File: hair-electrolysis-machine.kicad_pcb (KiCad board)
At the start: 2 copper layers, 53 x 53 mm, 98 parts, among them J1 USB_C_Receptacle_USB2.0_16P, J3 AudioJack2_Ground_Switch, J4 Conn_01x03_Pin, J5 Conn_01x03_Pin, J6 Conn_02x04_Odd_Even, J7 AudioJack2_Ground_Switch, Q1 BSS138, SW3 SW_SPDT, SW4 RotaryEncoder_Switch, SW5 RESET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

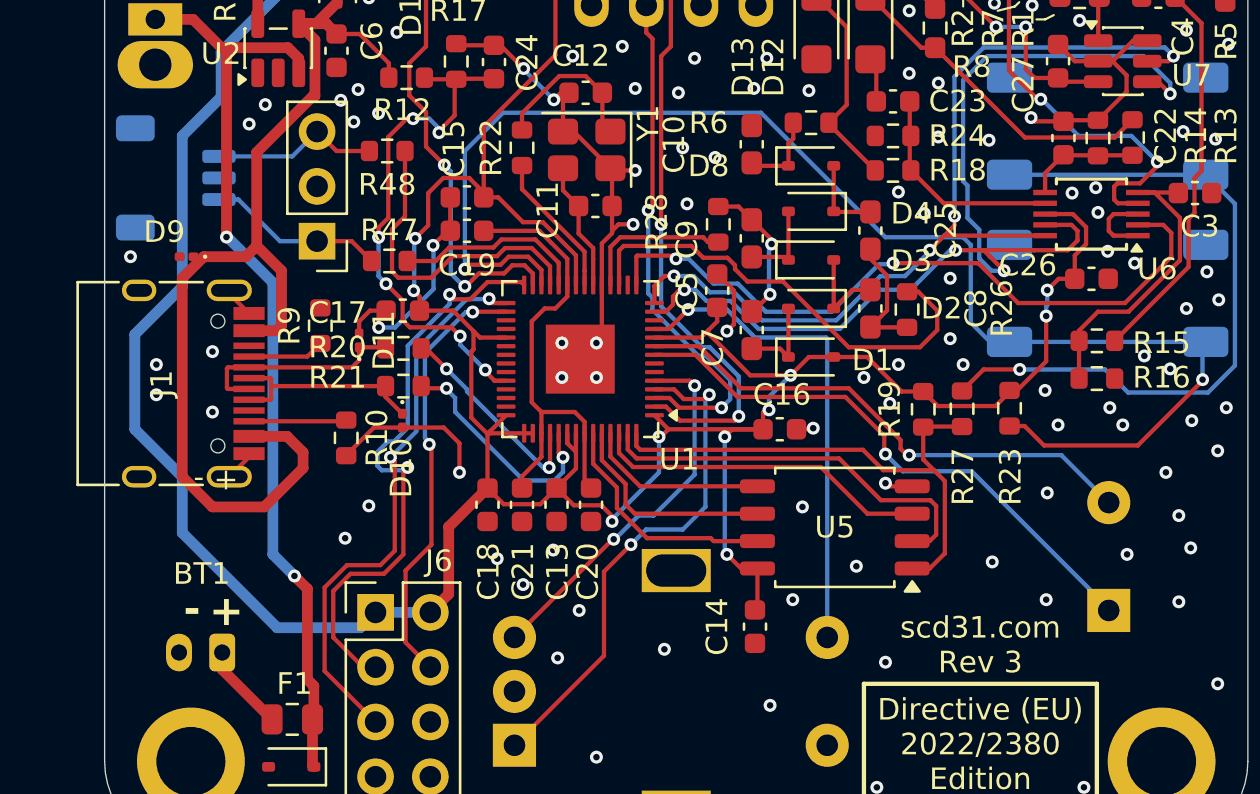
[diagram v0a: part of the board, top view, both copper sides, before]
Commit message: Minor changes
Moved 5v line out from under USB-C connector and changed buzzer pads so more common buzzers can more easily be used
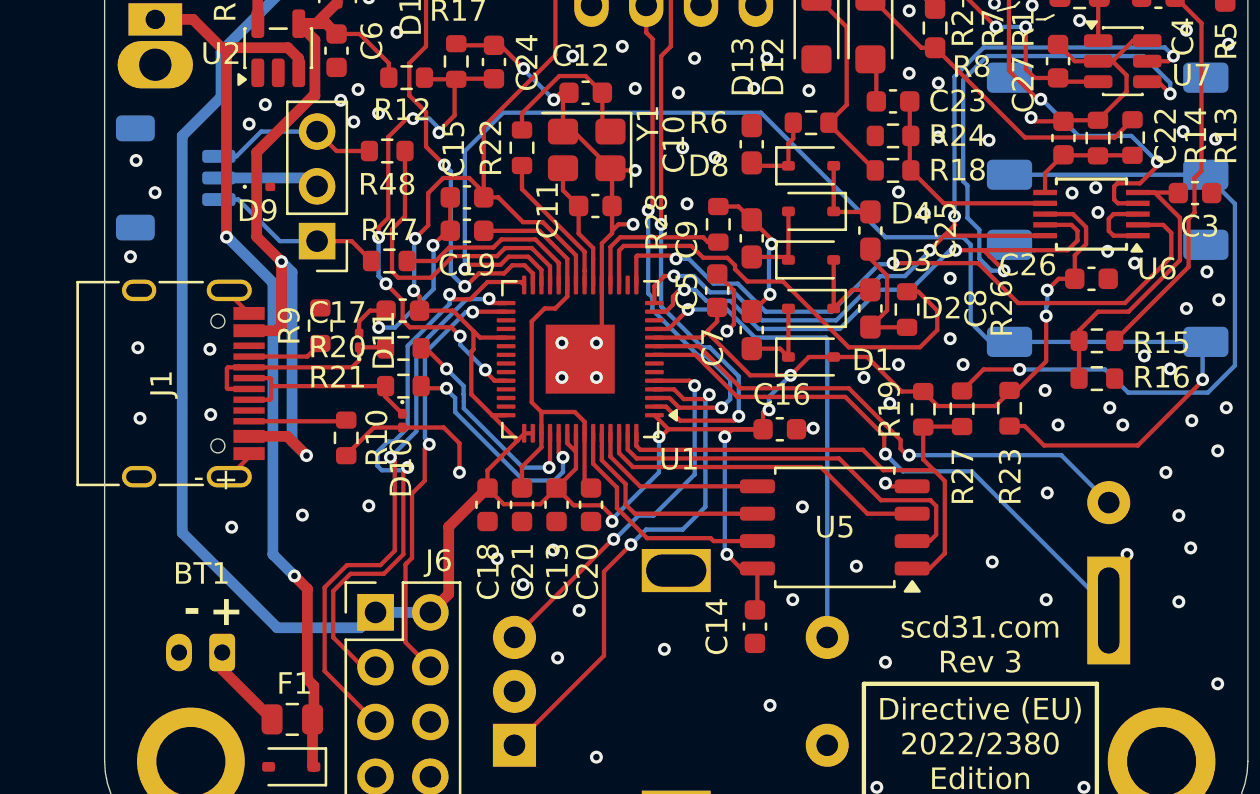
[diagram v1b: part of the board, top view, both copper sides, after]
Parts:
- moved D9 4.81 mm to (130.4, 93.4), turned to 0 degrees
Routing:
- net +5V: track 49.1 -> 37.9 mm, vias 0 -> 2
- net GND: track 71.8 -> 76.5 mm, vias 138 -> 141
- net +3.3V: track 223.0 -> 220.5 mm
- net Net-(U1-USB_DM): track 9.88 -> 10.4 mm

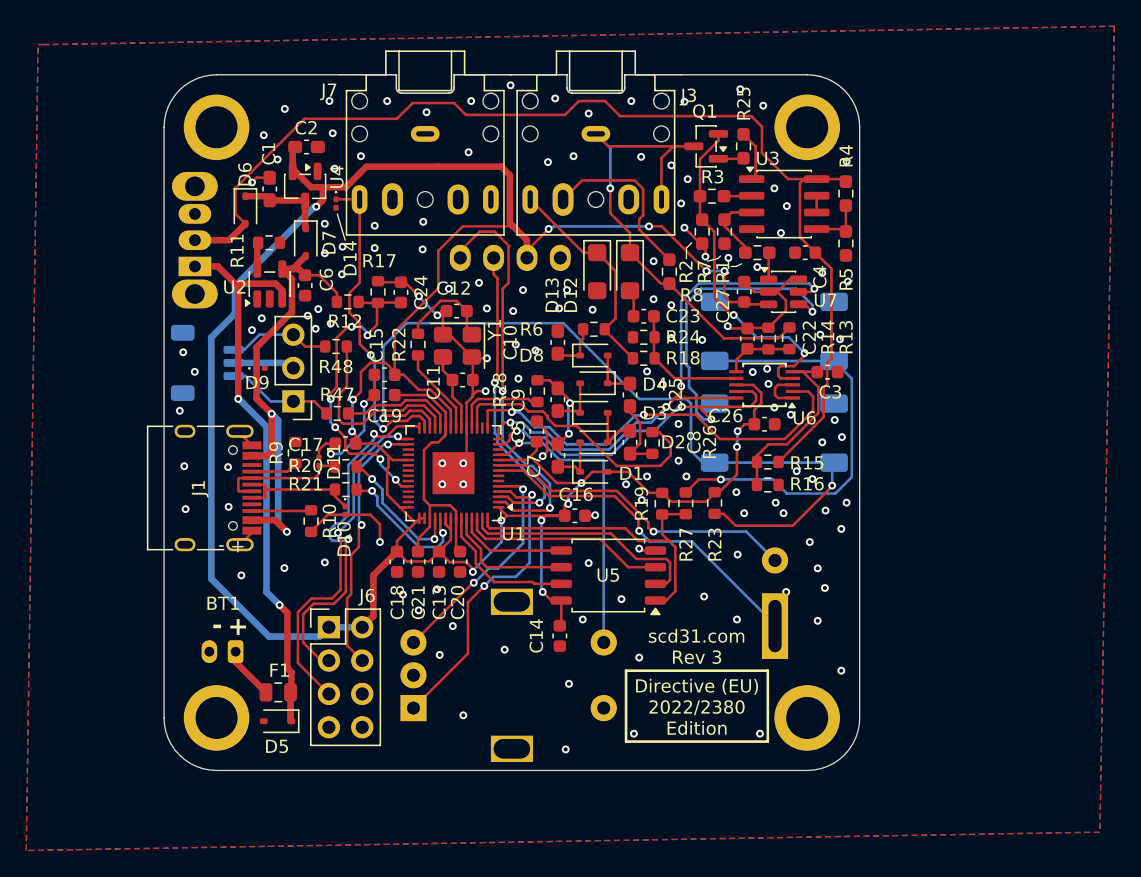
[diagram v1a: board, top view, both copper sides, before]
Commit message: Minor D9 ground changes
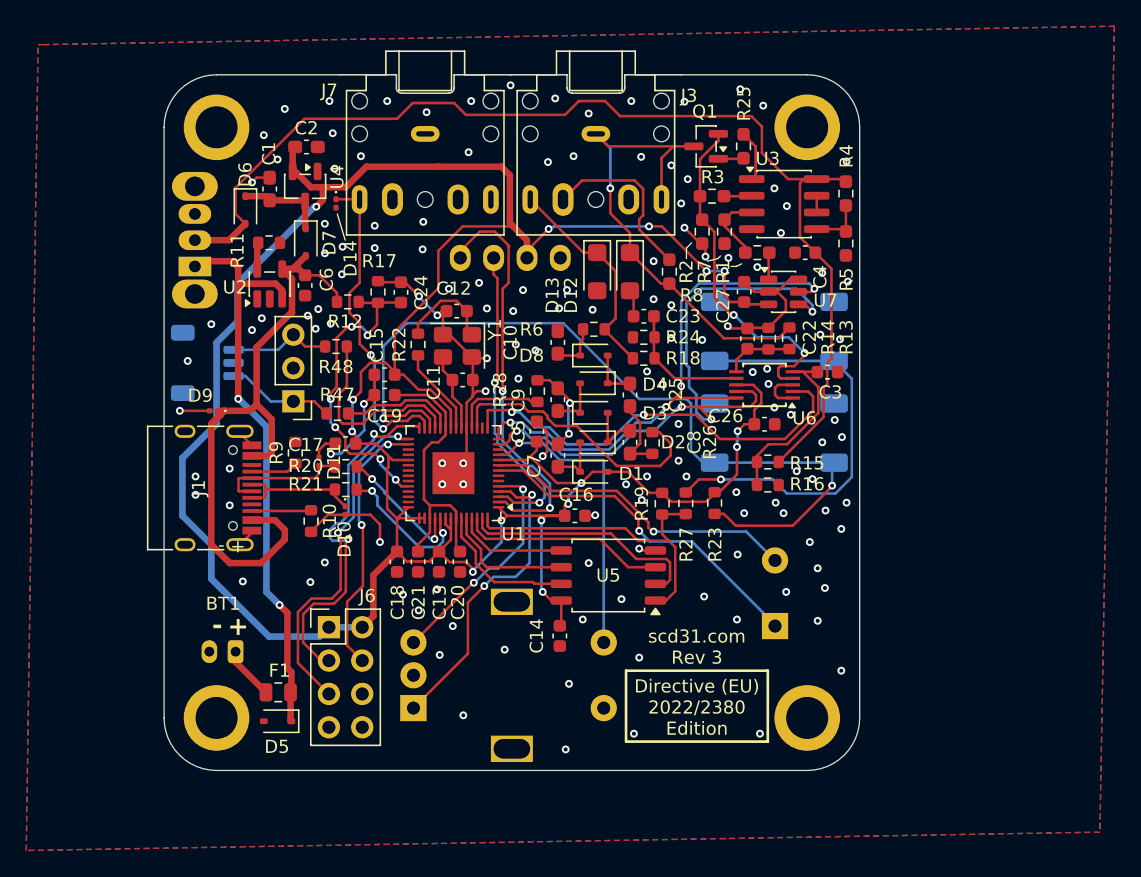
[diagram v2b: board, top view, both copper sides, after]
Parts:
- moved D9 4.81 mm to (126.8, 96.6), turned to 180 degrees
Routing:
- net +5V: track 37.9 -> 51.1 mm, vias 2 -> 0
- net +3.3V: track 220.5 -> 223.0 mm
- net GND: track 76.5 -> 74.1 mm
- net Net-(D5-K): track 43.2 -> 44.2 mm
- net Net-(U1-USB_DM): track 10.4 -> 9.88 mm

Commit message: Uploading the right version this time...
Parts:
- moved D9 4.81 mm to (130.4, 93.4), turned to 0 degrees
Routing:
- net +5V: track 51.1 -> 37.9 mm, vias 0 -> 2
- net GND: track 74.1 -> 78.7 mm, vias 141 -> 142
- net +3.3V: track 223.0 -> 220.3 mm
- net Net-(D5-K): track 44.2 -> 43.6 mm
- net Net-(U1-USB_DM): track 9.88 -> 10.4 mm
